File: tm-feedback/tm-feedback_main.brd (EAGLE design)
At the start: 100 x 80 mm, 1 part

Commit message: Add some intermodule connections
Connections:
- net BLUETOOTH1:GND renamed D_GND
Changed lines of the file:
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@@
 </elements>
 <signals>
-<signal name="BLUETOOTH1:GND">
+<signal name="BLUETOOTH1:VDD">
+<contactref element="BLUETOOTH1:U$1" pad="23"/>
+</signal>
+<signal name="D_GND">
 <contactref element="BLUETOOTH1:U$1" pad="9"/>
 <contactref element="BLUETOOTH1:U$1" pad="16"/>
@@
 <wire x1="13.37" y1="-21.18" x2="13.12" y2="-10.28" width="0" layer="19" extent="1-1"/>
 </signal>
-<signal name="BLUETOOTH1:VDD">
-<contactref element="BLUETOOTH1:U$1" pad="23"/>
-</signal>
 </signals>

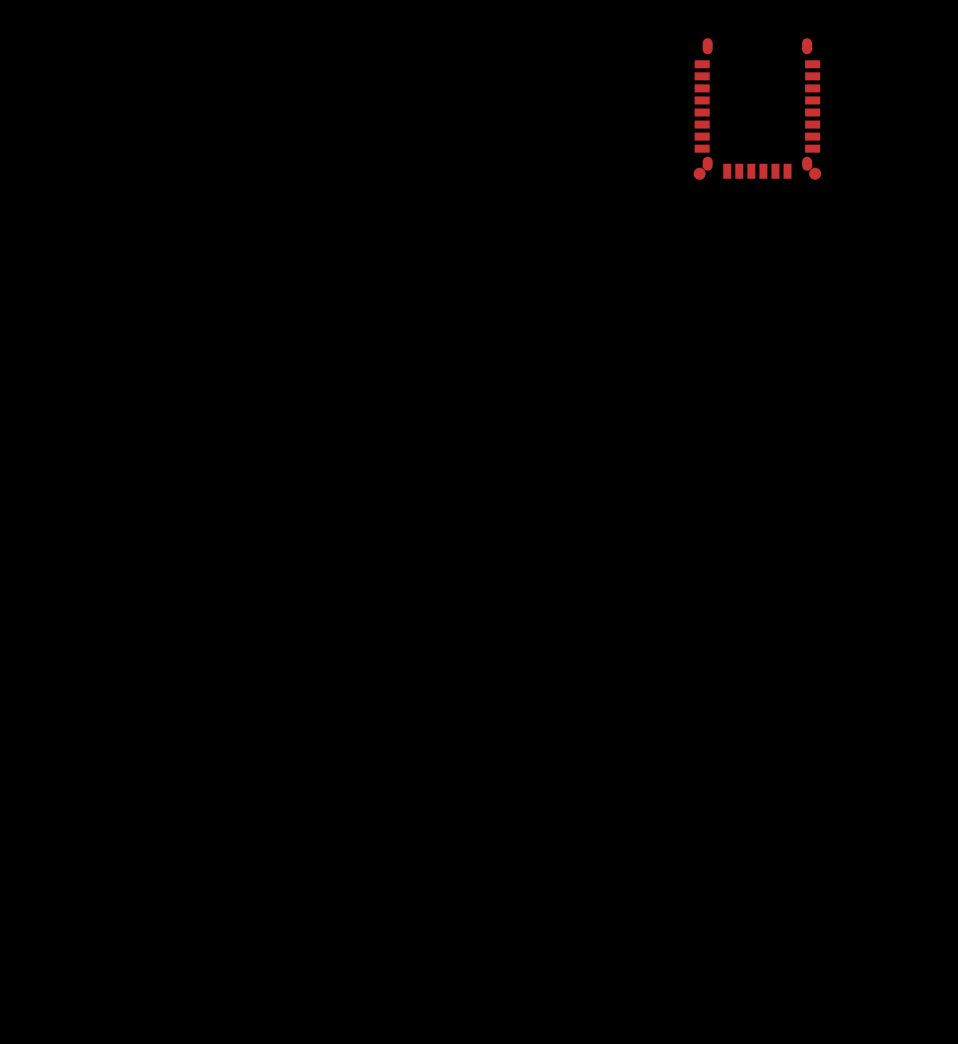
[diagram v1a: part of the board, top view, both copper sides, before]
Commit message: Add some components, complete motor driver
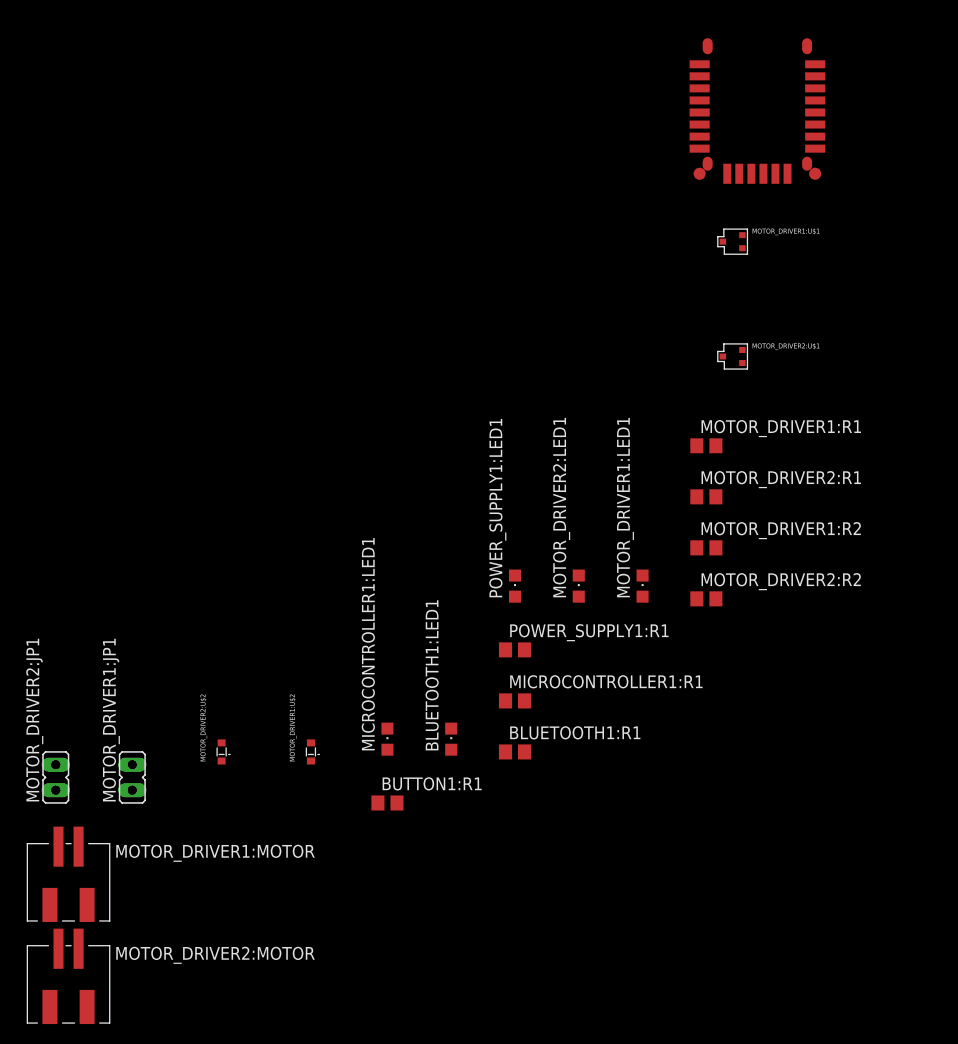
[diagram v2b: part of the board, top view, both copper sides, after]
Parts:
- added BLUETOOTH1:LED1, MICROCONTROLLER1:LED1, MOTOR_DRIVER1:LED1, MOTOR_DRIVER2:LED1, POWER_SUPPLY1:LED1: (no value), led:CHIPLED_0805
- added BLUETOOTH1:R1, BUTTON1:R1, MICROCONTROLLER1:R1, POWER_SUPPLY1:R1: (no value), resistor:R0805
- added MOTOR_DRIVER1:JP1, MOTOR_DRIVER2:JP1: (no value), jumper:JP1
- added MOTOR_DRIVER1:MOTOR, MOTOR_DRIVER2:MOTOR: JST-SMD-2, tactile-music:JST-SMD-2
- added MOTOR_DRIVER1:R1, MOTOR_DRIVER2:R1: 10k, rcl:R0805
- added MOTOR_DRIVER1:R2, MOTOR_DRIVER2:R2: (no value), rcl:R0805
- added MOTOR_DRIVER1:U$1, MOTOR_DRIVER2:U$1: PMF370XN, tactile-music:SOT323(SC-70)
- added MOTOR_DRIVER1:U$2, MOTOR_DRIVER2:U$2: DB2S308, tactile-music:SOD-523
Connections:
- new net A_3V3: MOTOR_DRIVER1:JP1.1, MOTOR_DRIVER1:MOTOR.1, MOTOR_DRIVER1:U$2.1, MOTOR_DRIVER2:JP1.1, MOTOR_DRIVER2:MOTOR.1, MOTOR_DRIVER2:U$2.1
- new net A_GND: MOTOR_DRIVER1:R1.1, MOTOR_DRIVER1:U$1.2, MOTOR_DRIVER2:R1.1, MOTOR_DRIVER2:U$1.2
- new net MOTOR_DRIVER1:N$1: MOTOR_DRIVER1:MOTOR.2, MOTOR_DRIVER1:R2.1, MOTOR_DRIVER1:U$1.3, MOTOR_DRIVER1:U$2.2
- new net MOTOR_DRIVER1:N$2: MOTOR_DRIVER1:JP1.2, MOTOR_DRIVER1:LED1.A
- new net MOTOR_DRIVER1:N$3: MOTOR_DRIVER1:LED1.C, MOTOR_DRIVER1:R2.2
- new net MOTOR_DRIVER2:N$1: MOTOR_DRIVER2:MOTOR.2, MOTOR_DRIVER2:R2.1, MOTOR_DRIVER2:U$1.3, MOTOR_DRIVER2:U$2.2
- new net MOTOR_DRIVER2:N$2: MOTOR_DRIVER2:JP1.2, MOTOR_DRIVER2:LED1.A
- new net MOTOR_DRIVER2:N$3: MOTOR_DRIVER2:LED1.C, MOTOR_DRIVER2:R2.2
- new net N$15: MOTOR_DRIVER1:R1.2, MOTOR_DRIVER1:U$1.1
- new net N$16: MOTOR_DRIVER2:R1.2, MOTOR_DRIVER2:U$1.1
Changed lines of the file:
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@@
 <layer number="97" name="Info" color="7" fill="1" visible="no" active="no"/>
 <layer number="98" name="Guide" color="6" fill="1" visible="no" active="no"/>
+<layer number="99" name="SpiceOrder" color="5" fill="1" visible="no" active="no"/>
 </layers>
 <board>
@@
 <elements>
 <element name="BLUETOOTH1:U$1" library="tactile-music" package="RN4020" value="RN4020" x="7.62" y="-11.43"/>
+<element name="MOTOR_DRIVER1:U$1" library="tactile-music" package="SOT323(SC-70)" value="PMF370XN" x="5.08" y="-27.94"/>
+<element name="MOTOR_DRIVER2:U$1" library="tactile-music" package="SOT323(SC-70)" value="PMF370XN" x="5.08" y="-39.37"/>
+<element name="MOTOR_DRIVER1:R1" library="rcl" package="R0805" value="10k" x="2.54" y="-48.26"/>
+<element name="MOTOR_DRIVER2:R1" library="rcl" package="R0805" value="10k" x="2.54" y="-53.34"/>
+<element name="MOTOR_DRIVER1:R2" library="rcl" package="R0805" value="" x="2.54" y="-58.42"/>
+<element name="MOTOR_DRIVER2:R2" library="rcl" package="R0805" value="" x="2.54" y="-63.5"/>
+<element name="MOTOR_DRIVER1:LED1" library="led" package="CHIPLED_0805" value="" x="-3.81" y="-62.23"/>
+<element name="MOTOR_DRIVER2:LED1" library="led" package="CHIPLED_0805" value="" x="-10.16" y="-62.23"/>
+<element name="POWER_SUPPLY1:LED1" library="led" package="CHIPLED_0805" value="" x="-16.51" y="-62.23"/>
+<element name="POWER_SUPPLY1:R1" library="resistor" package="R0805" value="" x="-16.51" y="-68.58"/>
+<element name="MICROCONTROLLER1:R1" library="resistor" package="R0805" value="" x="-16.51" y="-73.66"/>
+<element name="BLUETOOTH1:R1" library="resistor" package="R0805" value="" x="-16.51" y="-78.74"/>
+<element name="BLUETOOTH1:LED1" library="led" package="CHIPLED_0805" value="" x="-22.86" y="-77.47"/>
+<element name="MICROCONTROLLER1:LED1" library="led" package="CHIPLED_0805" value="" x="-29.21" y="-77.47"/>
+<element name="BUTTON1:R1" library="resistor" package="R0805" value="" x="-29.21" y="-83.82"/>
+<element name="MOTOR_DRIVER1:U$2" library="tactile-music" package="SOD-523" value="DB2S308" x="-36.83" y="-78.74"/>
+<element name="MOTOR_DRIVER2:U$2" library="tactile-music" package="SOD-523" value="DB2S308" x="-45.72" y="-78.74"/>
+<element name="MOTOR_DRIVER1:JP1" library="jumper" package="JP1" value="" x="-54.61" y="-81.28"/>
+<element name="MOTOR_DRIVER2:JP1" library="jumper" package="JP1" value="" x="-62.23" y="-81.28"/>
+<element name="MOTOR_DRIVER1:MOTOR" library="tactile-music" package="JST-SMD-2" value="JST-SMD-2" x="-60.96" y="-90.17"/>
+<element name="MOTOR_DRIVER2:MOTOR" library="tactile-music" package="JST-SMD-2" value="JST-SMD-2" x="-60.96" y="-100.33"/>
 </elements>
 <signals>
@@
 <contactref element="BLUETOOTH1:U$1" pad="1"/>
 <contactref element="BLUETOOTH1:U$1" pad="24"/>
-<wire x1="2.12" y1="-10.28" x2="1.87" y2="-21.18" width="0" layer="19" extent="1-1"/>
-<wire x1="13.12" y1="-10.28" x2="2.12" y2="-10.28" width="0" layer="19" extent="1-1"/>
-<wire x1="13.37" y1="-21.18" x2="13.12" y2="-10.28" width="0" layer="19" extent="1-1"/>
+<wire x1="1.87" y1="-10.28" x2="1.87" y2="-21.18" width="0" layer="19" extent="1-1"/>
+<wire x1="13.37" y1="-21.18" x2="1.87" y2="-21.18" width="0" layer="19" extent="1-1"/>
+<wire x1="13.37" y1="-10.28" x2="13.37" y2="-21.18" width="0" layer="19" extent="1-1"/>
+</signal>
+<signal name="A_3V3">
+<contactref element="MOTOR_DRIVER1:MOTOR" pad="1"/>
+<contactref element="MOTOR_DRIVER1:JP1" pad="1"/>
+<contactref element="MOTOR_DRIVER1:U$2" pad="1"/>
+<contactref element="MOTOR_DRIVER2:MOTOR" pad="1"/>
+<contactref element="MOTOR_DRIVER2:JP1" pad="1"/>
+<contactref element="MOTOR_DRIVER2:U$2" pad="1"/>
+<wire x1="-61.96" y1="-88.17" x2="-61.96" y2="-98.33" width="0" layer="19" extent="1-1"/>
+<wire x1="-62.23" y1="-82.55" x2="-61.96" y2="-88.17" width="0" layer="19" extent="1-1"/>
+<wire x1="-54.61" y1="-82.55" x2="-62.23" y2="-82.55" width="0" layer="19" extent="1-1"/>
+<wire x1="-45.72" y1="-79.64" x2="-54.61" y2="-82.55" width="0" layer="19" extent="1-1"/>
+<wire x1="-36.83" y1="-79.64" x2="-45.72" y2="-79.64" width="0" layer="19" extent="1-1"/>
+</signal>
+<signal name="MOTOR_DRIVER1:N$1">
+<contactref element="MOTOR_DRIVER1:MOTOR" pad="2"/>
+<contactref element="MOTOR_DRIVER1:U$1" pad="3"/>
+<contactref element="MOTOR_DRIVER1:R2" pad="1"/>
+<contactref element="MOTOR_DRIVER1:U$2" pad="2"/>
+<wire x1="-36.83" y1="-77.84" x2="-59.96" y2="-88.17" width="0" layer="19" extent="1-1"/>
+<wire x1="1.59" y1="-58.42" x2="-36.83" y2="-77.84" width="0" layer="19" extent="1-1"/>
+<wire x1="4.18" y1="-27.94" x2="1.59" y2="-58.42" width="0" layer="19" extent="1-1"/>
+</signal>
+<signal name="MOTOR_DRIVER2:N$1">
+<contactref element="MOTOR_DRIVER2:MOTOR" pad="2"/>
+<contactref element="MOTOR_DRIVER2:U$1" pad="3"/>
+<contactref element="MOTOR_DRIVER2:R2" pad="1"/>
+<contactref element="MOTOR_DRIVER2:U$2" pad="2"/>
+<wire x1="-45.72" y1="-77.84" x2="-59.96" y2="-98.33" width="0" layer="19" extent="1-1"/>
+<wire x1="1.59" y1="-63.5" x2="-45.72" y2="-77.84" width="0" layer="19" extent="1-1"/>
+<wire x1="4.18" y1="-39.37" x2="1.59" y2="-63.5" width="0" layer="19" extent="1-1"/>
+</signal>
+<signal name="MOTOR_DRIVER1:N$2">
+<contactref element="MOTOR_DRIVER1:JP1" pad="2"/>
+<contactref element="MOTOR_DRIVER1:LED1" pad="A"/>
+<wire x1="-3.81" y1="-63.28" x2="-54.61" y2="-80.01" width="0" layer="19" extent="1-1"/>
+</signal>
+<signal name="MOTOR_DRIVER2:N$2">
+<contactref element="MOTOR_DRIVER2:JP1" pad="2"/>
+<contactref element="MOTOR_DRIVER2:LED1" pad="A"/>
+<wire x1="-10.16" y1="-63.28" x2="-62.23" y2="-80.01" width="0" layer="19" extent="1-1"/>
+</signal>
+<signal name="MOTOR_DRIVER1:N$3">
+<contactref element="MOTOR_DRIVER1:LED1" pad="C"/>
+<contactref element="MOTOR_DRIVER1:R2" pad="2"/>
+<wire x1="3.49" y1="-58.42" x2="-3.81" y2="-61.18" width="0" layer="19" extent="1-1"/>
+</signal>
+<signal name="MOTOR_DRIVER2:N$3">
+<contactref element="MOTOR_DRIVER2:LED1" pad="C"/>
+<contactref element="MOTOR_DRIVER2:R2" pad="2"/>
+<wire x1="3.49" y1="-63.5" x2="-10.16" y2="-61.18" width="0" layer="19" extent="1-1"/>
+</signal>
+<signal name="A_GND">
+<contactref element="MOTOR_DRIVER1:U$1" pad="2"/>
+<contactref element="MOTOR_DRIVER2:U$1" pad="2"/>
+<contactref element="MOTOR_DRIVER1:R1" pad="1"/>
+<contactref element="MOTOR_DRIVER2:R1" pad="1"/>
+<wire x1="1.59" y1="-48.26" x2="1.59" y2="-53.34" width="0" layer="19" extent="1-1"/>
+<wire x1="6.13" y1="-38.72" x2="1.59" y2="-48.26" width="0" layer="19" extent="1-1"/>
+<wire x1="6.13" y1="-27.29" x2="6.13" y2="-38.72" width="0" layer="19" extent="1-1"/>
+</signal>
+<signal name="N$15">
+<contactref element="MOTOR_DRIVER1:U$1" pad="1"/>
+<contactref element="MOTOR_DRIVER1:R1" pad="2"/>
+<wire x1="6.13" y1="-28.59" x2="3.49" y2="-48.26" width="0" layer="19" extent="1-1"/>
+</signal>
+<signal name="N$16">
+<contactref element="MOTOR_DRIVER2:U$1" pad="1"/>
+<contactref element="MOTOR_DRIVER2:R1" pad="2"/>
+<wire x1="6.13" y1="-40.02" x2="3.49" y2="-53.34" width="0" layer="19" extent="1-1"/>
 </signal>
 </signals>

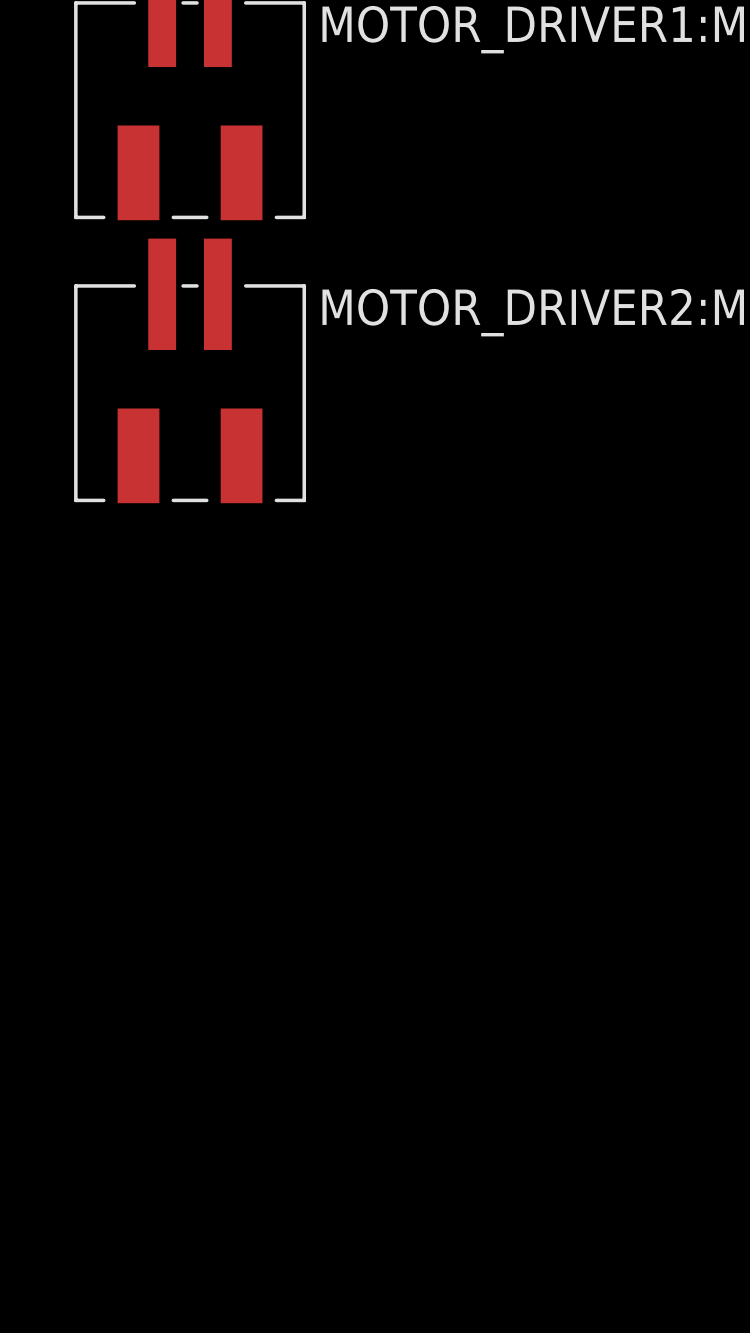
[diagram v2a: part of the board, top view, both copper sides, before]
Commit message: Add headers
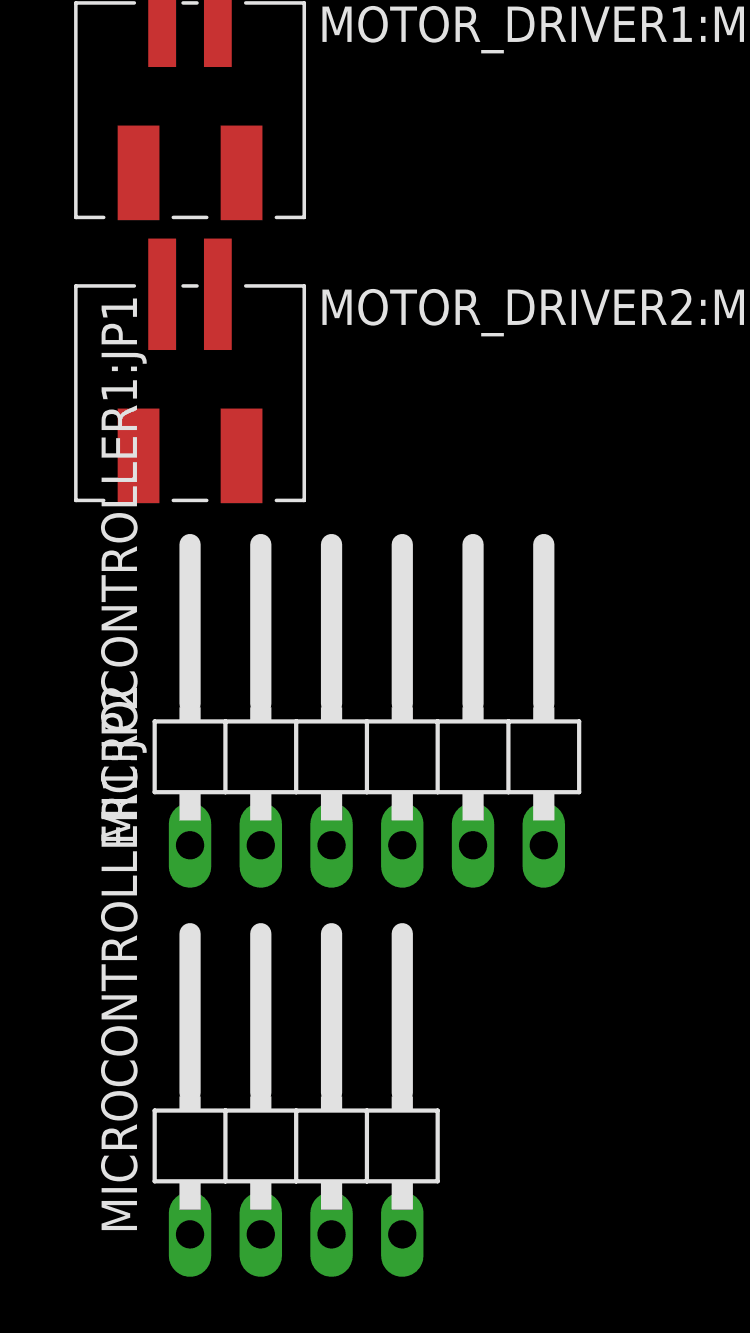
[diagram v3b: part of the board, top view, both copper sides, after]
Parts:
- added MICROCONTROLLER1:JP1: (no value), pinhead:1X06/90
- added MICROCONTROLLER1:JP2: (no value), pinhead:1X04/90
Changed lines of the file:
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@@
 <element name="MOTOR_DRIVER1:MOTOR" library="tactile-music" package="JST-SMD-2" value="JST-SMD-2" x="-60.96" y="-90.17"/>
 <element name="MOTOR_DRIVER2:MOTOR" library="tactile-music" package="JST-SMD-2" value="JST-SMD-2" x="-60.96" y="-100.33"/>
+<element name="MICROCONTROLLER1:JP1" library="pinhead" package="1X06/90" value="" x="-54.61" y="-114.3"/>
+<element name="MICROCONTROLLER1:JP2" library="pinhead" package="1X04/90" value="" x="-57.15" y="-128.27"/>
 </elements>
 <signals>
